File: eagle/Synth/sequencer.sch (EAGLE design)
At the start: 42 parts, among them IC1 LM741P, U1 ATMEGA328P_PDIP, U2 MAX5217GUA+, Y1 16MHz

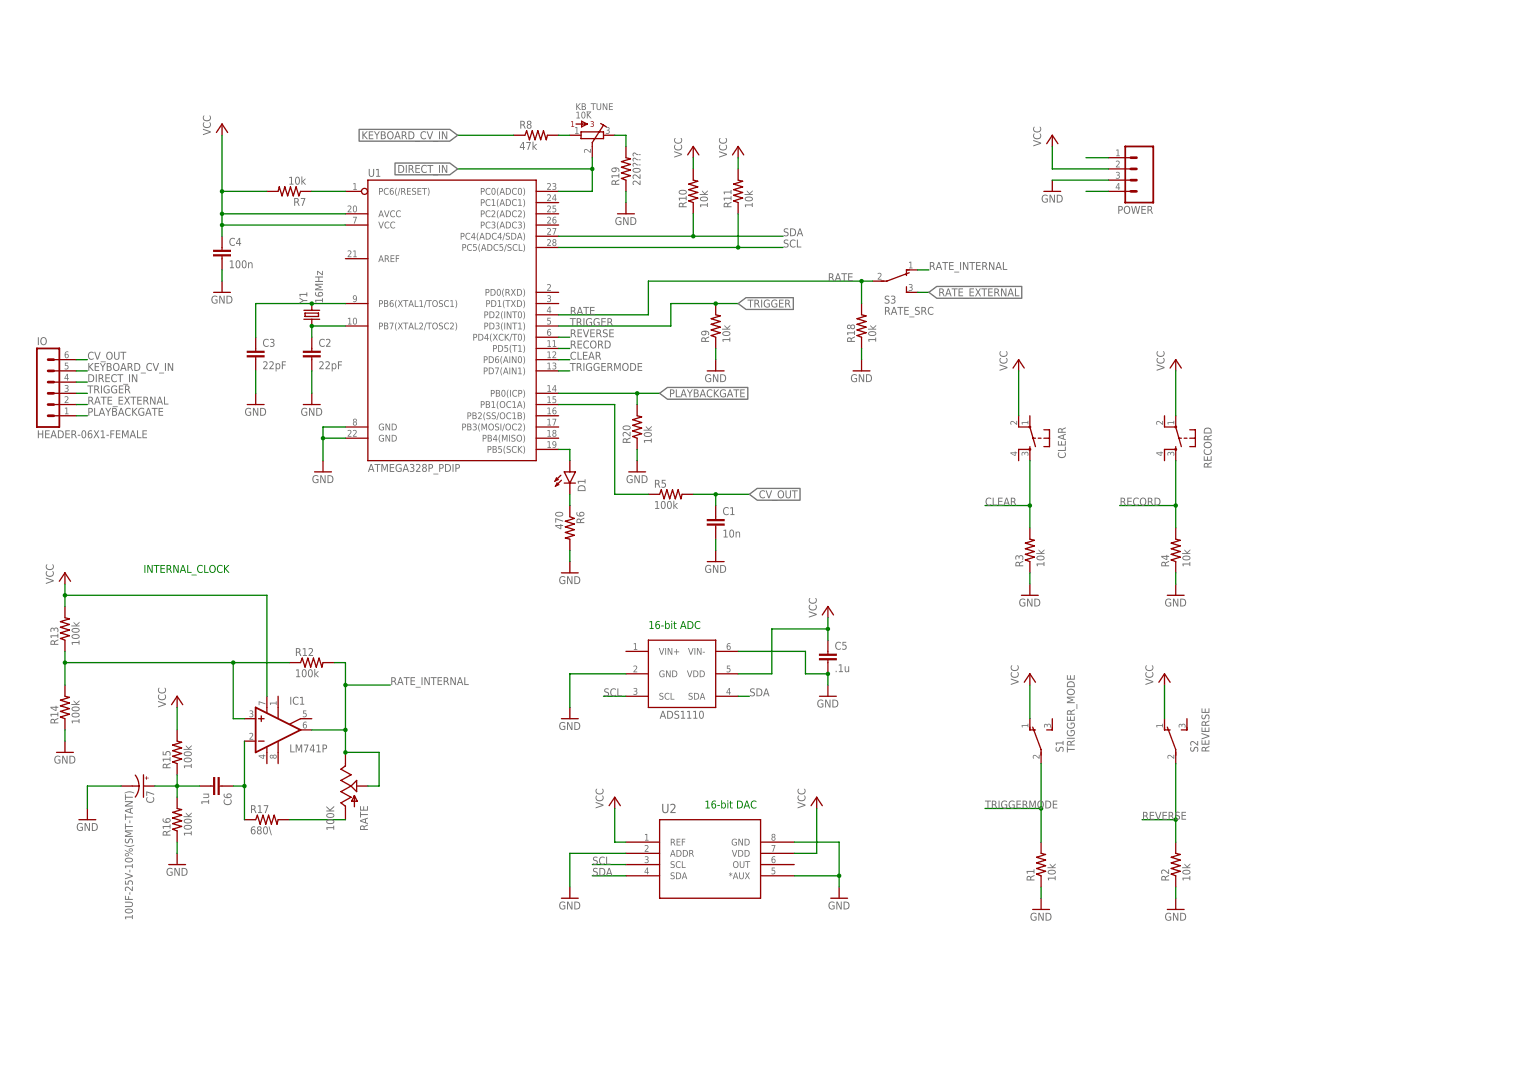
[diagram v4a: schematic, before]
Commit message: updated schematic for BOM
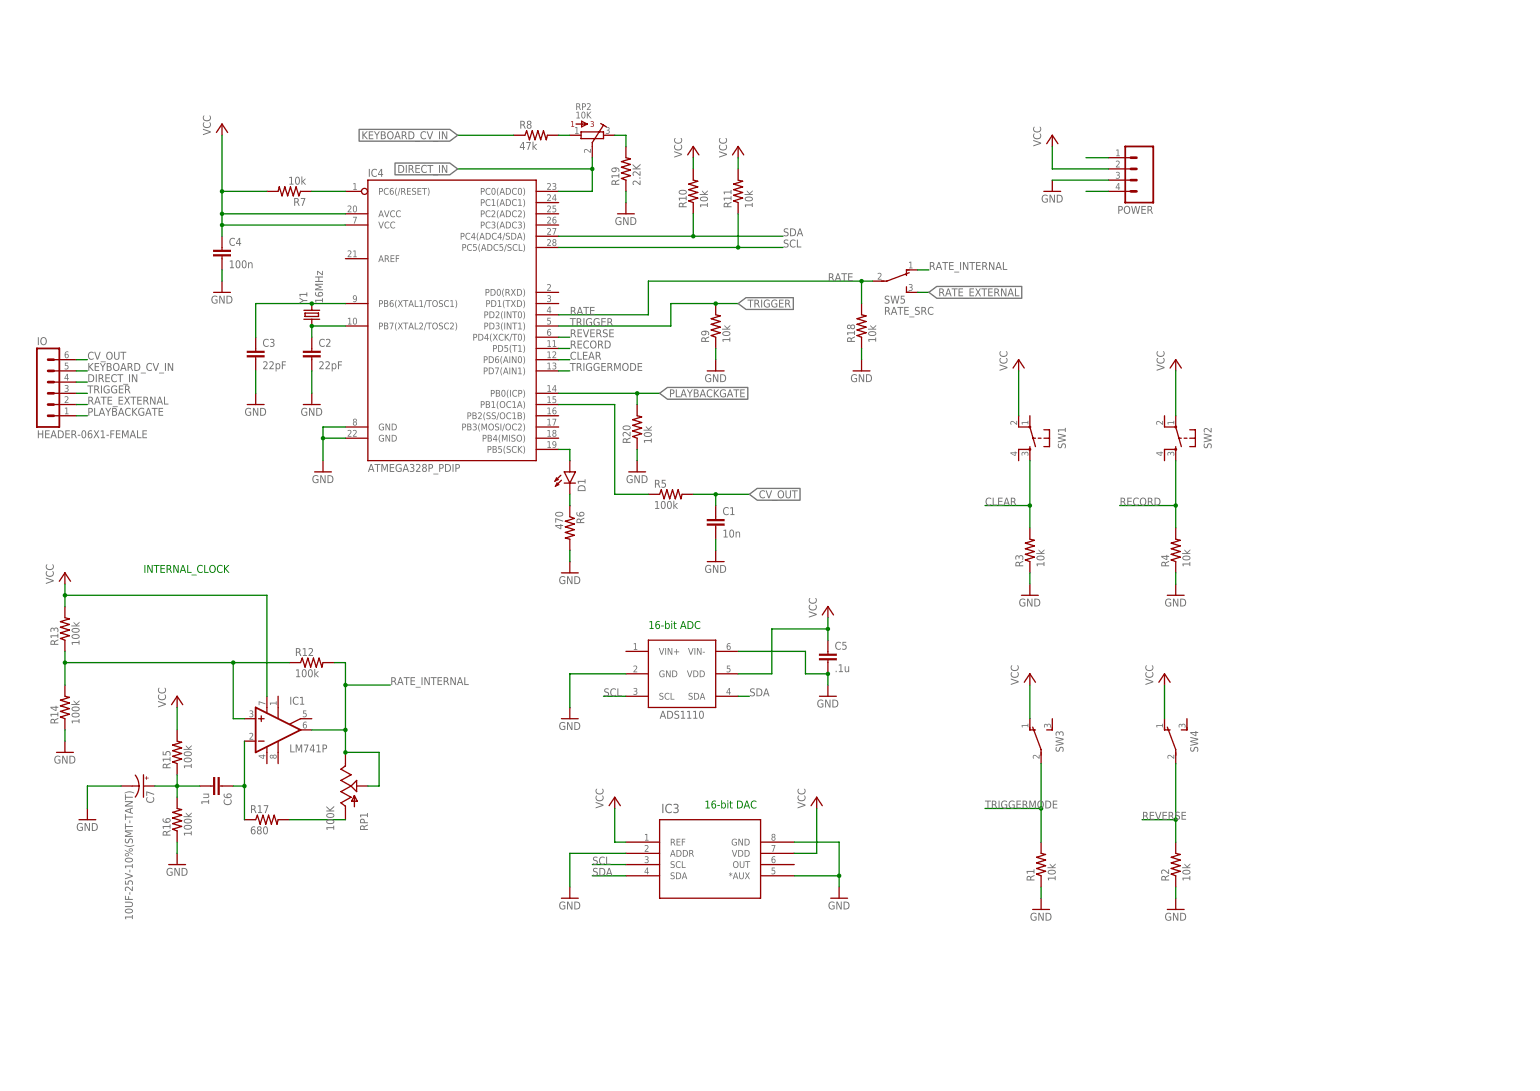
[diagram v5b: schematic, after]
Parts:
- R17: value 680\ -> 680
- R19: value 220??? -> 2.2K
- SW3: value TRIGGER_MODE -> TL36YO
- SW4: value REVERSE -> TL36YO
- renumbered CLEAR to SW1, KB_TUNE to RP2, RATE to RP1, RECORD to SW2, S1 to SW3, S2 to SW4, S3 to SW5, U1 to IC4, U2 to IC3
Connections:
- new net SW3: SW3.O
- net VCC: no longer SW3.O

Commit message: board tweaks
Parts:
- C4: value 100n -> .1u
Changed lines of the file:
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@@
 <part name="P+6" library="supply1" deviceset="VCC" device=""/>
 <part name="R7" library="SparkFun-Passives" deviceset="RESISTOR" device="1206" value="10k"/>
-<part name="C4" library="SparkFun-Capacitors" deviceset="CAP" device="1206" value="100n"/>
+<part name="C4" library="SparkFun-Capacitors" deviceset="CAP" device="1206" value=".1u"/>
 <part name="GND13" library="supply1" deviceset="GND" device=""/>
 <part name="R9" library="SparkFun-Passives" deviceset="RESISTOR" device="1206" value="10k"/>

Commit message: added other files
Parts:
- removed R19: 2.2K, SparkFun-Passives:RESISTOR1206
- removed R8: 47k, SparkFun-Passives:RESISTOR1206
- added RP3: 10K, bourns:3386-P
- IC3: value MAX5217GUA+ -> DAC8571; device cjk:MAX5217GUA+ -> cjk:DAC8571
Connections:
- removed net KEYBOARD_CV_IN: IO.5, R8.1
- removed net N$4: R8.2, RP2.1
- removed net SW3: SW3.O
- new net CV_IN: IO.5, RP2.1
- net CLEAR: now also SW1.4
- net CV_OUT: now also RP3.2
- net DIRECT_IN: now also IC2.VIN+; no longer IC4.PC0(ADC0), IO.4
- net GND: now also IC3.A0, RP2.3, RP3.3; no longer IC3.*AUX, IC3.ADDR, R19.1
- net N$2: now also IC3.VOUT, IC3.VSENSE, RP3.1; no longer R19.2, RP2.3
- net RECORD: now also IO.4, SW2.4
- net VCC: now also IC3.VREF, SW1.1, SW2.2, SW3.O; no longer IC3.REF
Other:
- moved on the sheet: RP2
